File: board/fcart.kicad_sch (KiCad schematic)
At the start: 95 parts, among them J1 JTAG, J2 USB4085, J3 MSD-4-A, J4 SWD, J5 Famicom_cartridge, SW1 PTS647SM70, U1 TPS2116, U10 LCMXO2-4000HC-4TG144C, U2 USBLC6-2SC6, U3 TLV76133DCY, U4 SN74ALVC164245DGG, U5 SN74ALVC164245DGG, U6 SN74ALVC164245DGG, U7 SN74ALVC164245DGG, U8 STM32F412RET6, U9 W9864G6KH-6, Y1 ABS07-32.768KHZ-7, Y2 ABM8W-12.0000MHZ-8-B1U, Y3 ASE-50.000MHZ-LC

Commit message: implementation of sound dac
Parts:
- removed R8: 100, Resistor_SMD:R_0805_2012Metric, symbol Device:R
- added C9: 0.1u, Capacitor_SMD:C_0805_2012Metric, symbol Device:C
- added R10: 47k, Resistor_SMD:R_0805_2012Metric, symbol Device:R
- added R9: 100k, Resistor_SMD:R_0805_2012Metric, symbol Device:R
- added U4: LM321, Package_TO_SOT_SMD:SOT-23-5, symbol Amplifier_Operational:LM321
- C10: renamed from C6; value 4.7u -> 10u
- C8: renamed from C7; value 0.1u -> 10n
- renumbered C8 to C1, C1 to C11, C5 to C12, C12 to C13, C13 to C14, C14 to C15, C15 to C16, C16 to C17, C17 to C18, C18 to C19, C19 to C20, C25 to C21, C26 to C22, C20 to C23, C21 to C24, C22 to C25, C27 to C26, C23 to C27, C24 to C28, C28 to C29, C9 to C3, C29 to C30, C30 to C31, C31 to C32, C32 to C33, C33 to C34, C46 to C35, C34 to C36, C35 to C37, C36 to C38, C37 to C39, C10 to C4, C38 to C40, C39 to C41, C40 to C42, C41 to C43, C42 to C44, C43 to C45, C44 to C46, C45 to C47, C47 to C48, C48 to C49, C11 to C5, C49 to C50, C50 to C51, C3 to C6, C4 to C7, J2 to J1, J3 to J2, J4 to J3, J1 to J4, R2 to R1, R10 to R11, R11 to R12, R4 to R2, R6 to R4, R9 to R6, R1 to R7, R7 to R8, U2 to U1, U9 to U11, U3 to U2, U1 to U3, U4 to U5, U5 to U6, U6 to U7, U7 to U8, U8 to U9
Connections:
- net GND: now also U7.43 (1A3), C9.1, R9.2, U4.2 (V-)
- net PPU_A0: now also U10.87 (PR10D/BANK1/C); no longer U10.89 (PR10C/BANK1/T)
- net PPU_A1: now also U10.85 (PR13B/BANK1/C/DQS1N); no longer U10.86 (PR13A/BANK1/T/DQS1)
- net PPU_A10: now also U10.82 (PR15A/BANK1/T/DQ1); no longer U10.83 (PR14B/BANK1/C/DQ1)
- net PPU_A11: now also U10.84 (PR14A/BANK1/T/DQ1); no longer U10.85 (PR13B/BANK1/C/DQS1N)
- net PPU_A12: now also U10.86 (PR13A/BANK1/T/DQS1); no longer U10.87 (PR10D/BANK1/C)
- net PPU_A13: now also U10.89 (PR10C/BANK1/T); no longer U10.91 (PR10B/BANK1/C/PCLKC1_0/DQ0)
- net PPU_A2: now also U10.83 (PR14B/BANK1/C/DQ1); no longer U10.84 (PR14A/BANK1/T/DQ1)
- net PPU_A3: now also U10.81 (PR15B/BANK1/C/DQ1); no longer U10.82 (PR15A/BANK1/T/DQ1)
- net PPU_A4: now also U10.77 (PR16B/BANK1/C/DQ1); no longer U10.78 (PR16A/BANK1/T/DQ1)
- net PPU_A5: now also U10.75 (PR18B/BANK1/C/DQ1); no longer U10.76 (PR18A/BANK1/T/DQ1)
- net PPU_A6: now also U10.73 (PR19B/BANK1/C/DQ1); no longer U10.74 (PR19A/BANK1/T/DQ1)
- net PPU_A7: now also U10.74 (PR19A/BANK1/T/DQ1); no longer U10.75 (PR18B/BANK1/C/DQ1)
- net PPU_A8: now also U10.76 (PR18A/BANK1/T/DQ1); no longer U10.77 (PR16B/BANK1/C/DQ1)
- net PPU_A9: now also U10.78 (PR16A/BANK1/T/DQ1); no longer U10.81 (PR15B/BANK1/C/DQ1)
- net PPU_D0: now also U10.91 (PR10B/BANK1/C/PCLKC1_0/DQ0); no longer U10.93 (PR9B/BANK1/C/DQS0N)
- net PPU_D1: now also U10.94 (PR9A/BANK1/T/DQS0); no longer U10.95 (PR8B/BANK1/C/DQ0)
- net PPU_D2: now also U10.96 (PR8A/BANK1/T/DQ0); no longer U10.97 (PR6B/BANK1/C/DQ0)
- net PPU_D3: now also U10.98 (PR6A/BANK1/T/DQ0); no longer U10.99 (PR5B/BANK1/C/DQ0)
- net PPU_D4: now also U10.99 (PR5B/BANK1/C/DQ0); no longer U10.100 (PR5A/BANK1/T/DQ0)
- net PPU_D5: now also U10.97 (PR6B/BANK1/C/DQ0); no longer U10.98 (PR6A/BANK1/T/DQ0)
- net PPU_D6: now also U10.95 (PR8B/BANK1/C/DQ0); no longer U10.96 (PR8A/BANK1/T/DQ0)
- net PPU_D7: now also U10.93 (PR9B/BANK1/C/DQS0N); no longer U10.94 (PR9A/BANK1/T/DQS0)
- net PPU_DIR: now also U10.100 (PR5A/BANK1/T/DQ0); no longer U10.103 (PR4C/BANK1)
- net PPU_RD: now also U10.69 (PB29B/BANK2/C); no longer U10.73 (PR19B/BANK1/C/DQ1)
- net PPU_WR: now also U10.68 (PB29A/BANK2/T); no longer U10.69 (PB29B/BANK2/C)
- net SDRAM_CAS: now also U10.23 (PL14A/BANK4/T); no longer U10.24 (PL14B/BANK4/C)
- net SDRAM_CS: now also U10.21 (PL13A/BANK4/T); no longer U10.22 (PL13B/BANK4/C)
- net SDRAM_DQ0: now also U10.11 (PL8A/BANK5/T); no longer U10.12 (PL8B/BANK5/C)
- net SDRAM_DQ1: now also U10.12 (PL8B/BANK5/C); no longer U10.13 (PL9A/BANK4/T)
- net SDRAM_DQ10: now also U10.3 (PL4A/BANK5/T/L_GPLLT_IN); no longer U10.4 (PL4B/BANK5/C/L_GPLLC_IN)
- net SDRAM_DQ11: now also U10.4 (PL4B/BANK5/C/L_GPLLC_IN); no longer U10.5 (PL6A/BANK5/T/PCLKT5_0)
- net SDRAM_DQ12: now also U10.5 (PL6A/BANK5/T/PCLKT5_0); no longer U10.6 (PL6B/BANK5/C/PCLKC5_0)
- net SDRAM_DQ13: now also U10.6 (PL6B/BANK5/C/PCLKC5_0); no longer U10.9 (PL7A/BANK5/T)
- net SDRAM_DQ14: now also U10.9 (PL7A/BANK5/T); no longer U10.10 (PL7B/BANK5/C)
- net SDRAM_DQ15: now also U10.10 (PL7B/BANK5/C); no longer U10.11 (PL8A/BANK5/T)
- net SDRAM_DQ2: now also U10.13 (PL9A/BANK4/T); no longer U10.14 (PL9B/BANK4/C)
- net SDRAM_DQ3: now also U10.14 (PL9B/BANK4/C); no longer U10.15 (PL10A/BANK4/T)
- net SDRAM_DQ4: now also U10.15 (PL10A/BANK4/T); no longer U10.17 (PL10B/BANK4/C)
- net SDRAM_DQ5: now also U10.17 (PL10B/BANK4/C); no longer U10.19 (PL10C/BANK4/T/PCLKT4_0)
- net SDRAM_DQ6: now also U10.19 (PL10C/BANK4/T/PCLKT4_0); no longer U10.20 (PL10D/BANK4/C/PCLKC4_0)
- net SDRAM_DQ7: now also U10.20 (PL10D/BANK4/C/PCLKC4_0); no longer U10.21 (PL13A/BANK4/T)
- net SDRAM_DQ8: now also U10.1 (PL3A/BANK5/T/L_GPLLT_FB); no longer U10.2 (PL3B/BANK5/C/L_GPLLC_FB)
- net SDRAM_DQ9: now also U10.2 (PL3B/BANK5/C/L_GPLLC_FB); no longer U10.3 (PL4A/BANK5/T/L_GPLLT_IN)
- net SDRAM_LDQM: now also U10.25 (PL16A/BANK3/T); no longer U10.26 (PL16B/BANK3/C)
- net SDRAM_RAS: now also U10.22 (PL13B/BANK4/C); no longer U10.23 (PL14A/BANK4/T)
- net SDRAM_UDQM: now also U10.119 (PT23D/BANK0/C/PROGRAMN); no longer U10.1 (PL3A/BANK5/T/L_GPLLT_FB)
- net SDRAM_WE: now also U10.24 (PL14B/BANK4/C); no longer U10.25 (PL16A/BANK3/T)
- net VCART: now also C9.2, U4.5 (V+)
- net at C8.1, R8.1: now also R9.1, U4.1 (+); no longer C10.1
- net SND_IN_5V renamed SND_MIX
- net SND_MIX: now also J5.46 (SND_OUT), R10.1
- net SND_OUT_5V: no longer names the net of C10.2
- net SND_OUT_5V: now also R10.2; no longer J5.46 (SND_OUT)
- removed net SND_SYN: U10.68 (PB29A/BANK2/T), U7.43 (1A3)
- net SND_SYN_5V: no longer names the net of U7.6 (1B3)
- net SND_SYN_5V: no longer R8.2
- new net: C10.1, U4.3 (-), U4.4
- new net SND_OUT: R8.2, U10.26 (PL16B/BANK3/C)
- no-connect marks 47 -> 48
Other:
- moved on the sheet: C10, C6, C7, C8, J2, J3, J4, R7, R8

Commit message: PCB: route USB VBUS signal
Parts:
- added R5: 10k, Resistor_SMD:R_0805_2012Metric, symbol Device:R
- renumbered R9 to R10, R10 to R11, R11 to R12, R12 to R13, R5 to R6, R6 to R7, R7 to R8, R8 to R9
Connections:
- net +3V3: now also R5.2
- net BTN: now also U9.17 (PA3); no longer U9.26 (PB0)
- net CIRAM_A10: now also U10.67 (PB27B/BANK2/C); no longer U10.65 (PB27A/BANK2/T)
- net CIRAM_CE: now also U10.68 (PB29A/BANK2/T); no longer U10.67 (PB27B/BANK2/C)
- net CPU_D0: now also U10.61 (PB24A/BANK2/T); no longer U10.60 (PB23B/BANK2/C)
- net CPU_D1: now also U10.60 (PB23B/BANK2/C); no longer U10.59 (PB23A/BANK2/T)
- net CPU_D2: now also U10.59 (PB23A/BANK2/T); no longer U10.58 (PB21B/BANK2/C)
- net CPU_D3: now also U10.58 (PB21B/BANK2/C); no longer U10.57 (PB21A/BANK2/T)
- net CPU_D4: now also U10.57 (PB21A/BANK2/T); no longer U10.56 (PB20B/BANK2/C/PCLKC2_1)
- net CPU_D5: now also U10.56 (PB20B/BANK2/C/PCLKC2_1); no longer U10.55 (PB20A/BANK2/T/PCLKT2_1)
- net CPU_RW: now also U10.63 (PB24D/BANK2); no longer U10.62 (PB24B/BANK2/C)
- net FPGA_IRQ: now also U10.111 (PT27B/BANK0/C/LVDS), U9.20 (PA4); no longer U10.117 (PT24A/BANK0/T/LVDS), U9.59 (PB7)
- net IRQ: now also U10.65 (PB27A/BANK2/T); no longer U10.63 (PB24D/BANK2)
- net LED: now also U9.58 (PB6); no longer U9.62 (PB9)
- net PPU_D1: now also U10.93 (PR9B/BANK1/C/DQS0N); no longer U10.94 (PR9A/BANK1/T/DQS0)
- net PPU_D2: now also U10.95 (PR8B/BANK1/C/DQ0); no longer U10.96 (PR8A/BANK1/T/DQ0)
- net PPU_D3: now also U10.97 (PR6B/BANK1/C/DQ0); no longer U10.98 (PR6A/BANK1/T/DQ0)
- net PPU_D4: now also U10.98 (PR6A/BANK1/T/DQ0); no longer U10.99 (PR5B/BANK1/C/DQ0)
- net PPU_D5: now also U10.96 (PR8A/BANK1/T/DQ0); no longer U10.97 (PR6B/BANK1/C/DQ0)
- net PPU_D6: now also U10.94 (PR9A/BANK1/T/DQS0); no longer U10.95 (PR8B/BANK1/C/DQ0)
- net PPU_D7: now also U10.92 (PR10A/BANK1/T/PCLKT1_0/DQ0); no longer U10.93 (PR9B/BANK1/C/DQS0N)
- net PPU_DIR: now also U10.99 (PR5B/BANK1/C/DQ0); no longer U10.100 (PR5A/BANK1/T/DQ0)
- net PPU_RD: now also U10.55 (PB20A/BANK2/T/PCLKT2_1); no longer U10.69 (PB29B/BANK2/C)
- net PPU_WR: now also U10.69 (PB29B/BANK2/C); no longer U10.68 (PB29A/BANK2/T)
- net QSPI_CLK: now also U10.126 (PT20C/BANK0/T/SCL/PCLKT0_0); no longer U10.92 (PR10A/BANK1/T/PCLKT1_0/DQ0)
- net QSPI_IO0: now also U9.22 (PA6); no longer U9.40 (PC9)
- net QSPI_IO1: now also U9.23 (PA7); no longer U9.51 (PC10)
- net QSPI_IO2: now also U10.114 (PT25A/BANK0/T/LVDS), U9.24 (PC4); no longer U10.111 (PT27B/BANK0/C/LVDS), U9.39 (PC8)
- net QSPI_IO3: now also U10.115 (PT24B/BANK0/C/LVDS), U9.25 (PC5); no longer U10.114 (PT25A/BANK0/T/LVDS), U9.15 (PA1)
- net QSPI_NCS: now also U10.110 (PT28C/BANK0/T/INITN), U9.52 (PC11); no longer U10.115 (PT24B/BANK0/C/LVDS), U9.58 (PB6)
- net ROMSEL: now also U10.62 (PB24B/BANK2/C); no longer U10.61 (PB24A/BANK2/T)
- net SDRAM_A11: now also U10.119 (PT23D/BANK0/C/PROGRAMN); no longer U10.120 (PT23C/BANK0/T/JTAGENB)
- net SDRAM_A6: now also U10.125 (PT20D/BANK0/C/SDA/PCLKC0_0); no longer U10.126 (PT20C/BANK0/T/SCL/PCLKT0_0)
- net SDRAM_A7: now also U10.122 (PT21A/BANK0/T/LVDS); no longer U10.125 (PT20D/BANK0/C/SDA/PCLKC0_0)
- net SDRAM_A8: now also U10.121 (PT21B/BANK0/C/LVDS); no longer U10.122 (PT21A/BANK0/T/LVDS)
- net SDRAM_A9: now also U10.120 (PT23C/BANK0/T/JTAGENB); no longer U10.121 (PT21B/BANK0/C/LVDS)
- net SDRAM_UDQM: now also U10.117 (PT24A/BANK0/T/LVDS); no longer U10.119 (PT23D/BANK0/C/PROGRAMN)
- net SD_DAT1: now also U9.40 (PC9); no longer U9.41 (PA8)
- net SD_DAT2: now also U9.51 (PC10); no longer U9.42 (PA9)
- net SPI_MISO: now also U9.10 (PC2); no longer U9.22 (PA6)
- net SPI_MOSI: now also U9.11 (PC3); no longer U9.23 (PA7)
- net SPI_NCS: now also U9.16 (PA2); no longer U9.24 (PC4)
- net SPI_SCK: now also U9.38 (PC7); no longer U9.21 (PA5)
- net VBUS: now reaches U3.8 (ST)
- net VBUS: now also U9.42 (PA9), R5.1
- no-connect marks 48 -> 46
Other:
- moved on the sheet: D1, R6, R7, SW1

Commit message: Simplify power mux and improve audio
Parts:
- removed C10: 10u, Capacitor_SMD:C_0805_2012Metric, symbol Device:C
- removed U3: TPS2116, Package_TO_SOT_SMD:SOT-583-8, symbol Power_Management:TPS2116DRL
- removed U4: LM321, Package_TO_SOT_SMD:SOT-23-5, symbol Amplifier_Operational:LM321
- added C11: 47u, Capacitor_SMD:C_1206_3216Metric, symbol Device:C
- added C8: 0.1u, Capacitor_SMD:C_0805_2012Metric, symbol Device:C
- added D1, D2: MBR120, Diode_SMD:D_SOD-123F, symbol Device:D_Schottky
- added Q1: DTC114E, Package_TO_SOT_SMD:SOT-23-3, symbol Transistor_BJT:DTC114E
- added R12: 10k, Resistor_SMD:R_0805_2012Metric, symbol Device:R
- added U3: 74LVC1G3157, Package_TO_SOT_SMD:SOT-23-6, symbol 74xGxx:74LVC1G3157
- added U4: MCP6001, Package_TO_SOT_SMD:SOT-23-5, symbol Amplifier_Operational:MCP6001-OT
- C1: renamed from C4; value 1u -> 10u
- C2: renamed from C5; value 4.7u -> 10u
- C5: renamed from C2; value 10u -> 0.1u
- R10: value 100k -> 2.2k
- R11: value 47k -> 1k
- R3: value 10k -> 5.1k
- R4: value 5.1k -> 10k
- renumbered C9 to C10, C11 to C12, C12 to C13, C13 to C14, C14 to C15, C15 to C16, C16 to C17, C17 to C18, C18 to C19, C19 to C20, C20 to C21, C21 to C22, C22 to C23, C23 to C24, C24 to C25, C25 to C26, C26 to C27, C27 to C28, C28 to C29, C1 to C3, C29 to C30, C30 to C31, C31 to C32, C32 to C33, C33 to C34, C34 to C35, C35 to C36, C36 to C37, C37 to C38, C38 to C39, C3 to C4, C39 to C40, C40 to C41, C41 to C42, C42 to C43, C43 to C44, C44 to C45, C45 to C46, C46 to C47, C47 to C48, C48 to C49, C49 to C50, C50 to C51, C51 to C52, C8 to C9, D1 to D3, R12 to R13, R13 to R14
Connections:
- net +3V3: now also R5.1, C8.2, R12.2, U3.5 (VCC); no longer R5.2
- net +5V: now also D1.1 (K), D2.1 (K)
- net CIRAM_A10: now also U10.68 (PB29A/BANK2/T); no longer U10.67 (PB27B/BANK2/C)
- net CIRAM_CE: now also U10.69 (PB29B/BANK2/C); no longer U10.68 (PB29A/BANK2/T)
- net GND: now also C8.1, Q1.2 (E), U3.2 (GND), U4.2 (V-); no longer R10.2, U5.25 (2~{OE}), U5.48 (1~{OE}), U6.25 (2~{OE}), U6.48 (1~{OE}), U7.25 (2~{OE}), U7.48 (1~{OE}), U8.25 (2~{OE}), U8.48 (1~{OE})
- net IRQ: now also U10.67 (PB27B/BANK2/C); no longer U10.65 (PB27A/BANK2/T)
- net PPU_A0: now also U10.89 (PR10C/BANK1/T); no longer U10.87 (PR10D/BANK1/C)
- net PPU_A1: now also U10.86 (PR13A/BANK1/T/DQS1); no longer U10.85 (PR13B/BANK1/C/DQS1N)
- net PPU_A10: now also U10.83 (PR14B/BANK1/C/DQ1); no longer U10.82 (PR15A/BANK1/T/DQ1)
- net PPU_A11: now also U10.85 (PR13B/BANK1/C/DQS1N); no longer U10.84 (PR14A/BANK1/T/DQ1)
- net PPU_A12: now also U10.87 (PR10D/BANK1/C); no longer U10.86 (PR13A/BANK1/T/DQS1)
- net PPU_A13: now also U10.91 (PR10B/BANK1/C/PCLKC1_0/DQ0); no longer U10.89 (PR10C/BANK1/T)
- net PPU_A2: now also U10.84 (PR14A/BANK1/T/DQ1); no longer U10.83 (PR14B/BANK1/C/DQ1)
- net PPU_A3: now also U10.82 (PR15A/BANK1/T/DQ1); no longer U10.81 (PR15B/BANK1/C/DQ1)
- net PPU_A4: now also U10.78 (PR16A/BANK1/T/DQ1); no longer U10.77 (PR16B/BANK1/C/DQ1)
- net PPU_A5: now also U10.76 (PR18A/BANK1/T/DQ1); no longer U10.75 (PR18B/BANK1/C/DQ1)
- net PPU_A6: now also U10.74 (PR19A/BANK1/T/DQ1); no longer U10.73 (PR19B/BANK1/C/DQ1)
- net PPU_A7: now also U10.75 (PR18B/BANK1/C/DQ1); no longer U10.74 (PR19A/BANK1/T/DQ1)
- net PPU_A8: now also U10.77 (PR16B/BANK1/C/DQ1); no longer U10.76 (PR18A/BANK1/T/DQ1)
- net PPU_A9: now also U10.81 (PR15B/BANK1/C/DQ1); no longer U10.78 (PR16A/BANK1/T/DQ1)
- net PPU_D0: now also U10.92 (PR10A/BANK1/T/PCLKT1_0/DQ0); no longer U10.91 (PR10B/BANK1/C/PCLKC1_0/DQ0)
- net PPU_D1: now also U10.94 (PR9A/BANK1/T/DQS0); no longer U10.93 (PR9B/BANK1/C/DQS0N)
- net PPU_D2: now also U10.96 (PR8A/BANK1/T/DQ0); no longer U10.95 (PR8B/BANK1/C/DQ0)
- net PPU_D3: now also U10.98 (PR6A/BANK1/T/DQ0); no longer U10.97 (PR6B/BANK1/C/DQ0)
- net PPU_D4: now also U10.99 (PR5B/BANK1/C/DQ0); no longer U10.98 (PR6A/BANK1/T/DQ0)
- net PPU_D5: now also U10.97 (PR6B/BANK1/C/DQ0); no longer U10.96 (PR8A/BANK1/T/DQ0)
- net PPU_D6: now also U10.95 (PR8B/BANK1/C/DQ0); no longer U10.94 (PR9A/BANK1/T/DQS0)
- net PPU_D7: now also U10.93 (PR9B/BANK1/C/DQS0N); no longer U10.92 (PR10A/BANK1/T/PCLKT1_0/DQ0)
- net PPU_DIR: now also U10.100 (PR5A/BANK1/T/DQ0); no longer U10.99 (PR5B/BANK1/C/DQ0)
- net PPU_WR: now also U10.73 (PR19B/BANK1/C/DQ1); no longer U10.69 (PB29B/BANK2/C)
- net SND_OUT: now also J5.46 (SND_OUT), U3.4; no longer R9.2, U10.26 (PL16B/BANK3/C)
- net VCART: now also D1.2 (A), Q1.1 (B), U4.5 (V+)
- net VUSB: now also D2.2 (A)
- net at R11.2: now also C11.2
- net at C9.1, R9.1: now also U4.3 (+); no longer R10.1
- net USB_DET: now reaches R3.1, R4.2
- net USB_DET: now also U9.42 (PA9)
- removed net SND_MIX: J5.45 (SND_IN), J5.46 (SND_OUT), R11.1
- removed net VBUS: R5.1, U9.42 (PA9)
- new net: C11.1, U4.1, U4.4 (-)
- new net: R10.1, R11.1, U3.3
- new net LS_OE: Q1.3 (C), R5.2, U5.25 (2~{OE}), U5.48 (1~{OE}), U6.25 (2~{OE}), U6.48 (1~{OE}), U7.25 (2~{OE}), U7.48 (1~{OE}), U8.25 (2~{OE}), U8.48 (1~{OE})
- new net PDM: R9.2, U10.26 (PL16B/BANK3/C)
- new net SND_BYP: R12.1, U10.65 (PB27A/BANK2/T), U3.6
- new net SND_IN: J5.45 (SND_IN), R10.2, U3.1
- no-connect marks 46 -> 45
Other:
- moved on the sheet: BT1, C1, C10, C12, C13, C2, C3, C4, C5, C9, D3, R11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

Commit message: pcb: redesign audio circuit with active inverting mixer
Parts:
- removed C8: 0.1u, Capacitor_SMD:C_0805_2012Metric, symbol Device:C
- removed R12: 10k, Resistor_SMD:R_0805_2012Metric, symbol Device:R
- removed U3: 74LVC1G3157, Package_TO_SOT_SMD:SOT-23-6, symbol 74xGxx:74LVC1G3157
- added C11, C9: 4.7u, Capacitor_SMD:C_0805_2012Metric, symbol Device:C
- added C12: 0.1u, Capacitor_SMD:C_0805_2012Metric, symbol Device:C
- added C13: 6.8p, Capacitor_SMD:C_0805_2012Metric, symbol Device:C
- added JP1: SND-IN-OUT, Jumper:SolderJumper-2_P1.3mm_Open_RoundedPad1.0x1.5mm, symbol Jumper:SolderJumper_2_Open
- added R10, R14: 10k, Resistor_SMD:R_0805_2012Metric, symbol Device:R
- added R11: 5.1k, Resistor_SMD:R_0805_2012Metric, symbol Device:R
- added R13: 100k, Resistor_SMD:R_0805_2012Metric, symbol Device:R
- C10: value 0.1u -> 4.7u
- R12: renamed from R10; value 2.2k -> 100k
- R15: renamed from R11; value 1k -> 10k
- renumbered C11 to C14, C12 to C15, C13 to C16, C14 to C17, C15 to C18, C16 to C19, C17 to C20, C18 to C21, C19 to C22, C20 to C23, C21 to C24, C22 to C25, C23 to C26, C24 to C27, C25 to C28, C26 to C29, C27 to C30, C28 to C31, C29 to C32, C30 to C33, C31 to C34, C32 to C35, C33 to C36, C34 to C37, C35 to C38, C36 to C39, C37 to C40, C38 to C41, C39 to C42, C40 to C43, C41 to C44, C42 to C45, C43 to C46, C44 to C47, C45 to C48, C46 to C49, C47 to C50, C48 to C51, C49 to C52, C50 to C53, C51 to C54, C52 to C55, C9 to C8, R13 to R16, R14 to R17, U11 to U10, U4 to U3, U5 to U4, U6 to U5, U7 to U6, U8 to U7, U9 to U8, U10 to U9
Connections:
- net SND_BYP is gone; now on net IRQ: U9.65 (PB27A/BANK2/T)
- net +3V3: now also R12.2, U3.5 (V+), C12.2
- net CIRAM_A10: now also U9.67 (PB27B/BANK2/C); no longer U9.68 (PB29A/BANK2/T)
- net CIRAM_CE: now also U9.68 (PB29A/BANK2/T); no longer U9.69 (PB29B/BANK2/C)
- net GND: now also R15.2, C11.1, C12.1, R13.1; no longer C10.1
- net IRQ: no longer U9.67 (PB27B/BANK2/C)
- net PPU_A0: now also U9.87 (PR10D/BANK1/C); no longer U9.89 (PR10C/BANK1/T)
- net PPU_A1: now also U9.85 (PR13B/BANK1/C/DQS1N); no longer U9.86 (PR13A/BANK1/T/DQS1)
- net PPU_A10: now also U9.82 (PR15A/BANK1/T/DQ1); no longer U9.83 (PR14B/BANK1/C/DQ1)
- net PPU_A11: now also U9.84 (PR14A/BANK1/T/DQ1); no longer U9.85 (PR13B/BANK1/C/DQS1N)
- net PPU_A12: now also U9.86 (PR13A/BANK1/T/DQS1); no longer U9.87 (PR10D/BANK1/C)
- net PPU_A13: now also U9.89 (PR10C/BANK1/T); no longer U9.91 (PR10B/BANK1/C/PCLKC1_0/DQ0)
- net PPU_A2: now also U9.83 (PR14B/BANK1/C/DQ1); no longer U9.84 (PR14A/BANK1/T/DQ1)
- net PPU_A3: now also U9.81 (PR15B/BANK1/C/DQ1); no longer U9.82 (PR15A/BANK1/T/DQ1)
- net PPU_A4: now also U9.77 (PR16B/BANK1/C/DQ1); no longer U9.78 (PR16A/BANK1/T/DQ1)
- net PPU_A5: now also U9.75 (PR18B/BANK1/C/DQ1); no longer U9.76 (PR18A/BANK1/T/DQ1)
- net PPU_A6: now also U9.73 (PR19B/BANK1/C/DQ1); no longer U9.74 (PR19A/BANK1/T/DQ1)
- net PPU_A7: now also U9.74 (PR19A/BANK1/T/DQ1); no longer U9.75 (PR18B/BANK1/C/DQ1)
- net PPU_A8: now also U9.76 (PR18A/BANK1/T/DQ1); no longer U9.77 (PR16B/BANK1/C/DQ1)
- net PPU_A9: now also U9.78 (PR16A/BANK1/T/DQ1); no longer U9.81 (PR15B/BANK1/C/DQ1)
- net PPU_D0: now also U9.91 (PR10B/BANK1/C/PCLKC1_0/DQ0); no longer U9.92 (PR10A/BANK1/T/PCLKT1_0/DQ0)
- net PPU_D1: now also U9.93 (PR9B/BANK1/C/DQS0N); no longer U9.94 (PR9A/BANK1/T/DQS0)
- net PPU_D2: now also U9.95 (PR8B/BANK1/C/DQ0); no longer U9.96 (PR8A/BANK1/T/DQ0)
- net PPU_D3: now also U9.97 (PR6B/BANK1/C/DQ0); no longer U9.98 (PR6A/BANK1/T/DQ0)
- net PPU_D4: now also U9.98 (PR6A/BANK1/T/DQ0); no longer U9.99 (PR5B/BANK1/C/DQ0)
- net PPU_D5: now also U9.96 (PR8A/BANK1/T/DQ0); no longer U9.97 (PR6B/BANK1/C/DQ0)
- net PPU_D6: now also U9.94 (PR9A/BANK1/T/DQS0); no longer U9.95 (PR8B/BANK1/C/DQ0)
- net PPU_D7: now also U9.92 (PR10A/BANK1/T/PCLKT1_0/DQ0); no longer U9.93 (PR9B/BANK1/C/DQS0N)
- net PPU_DIR: now also U9.99 (PR5B/BANK1/C/DQ0); no longer U9.100 (PR5A/BANK1/T/DQ0)
- net PPU_WR: now also U9.69 (PB29B/BANK2/C); no longer U9.73 (PR19B/BANK1/C/DQ1)
- net SND_IN: now also C9.1, JP1.1 (A); no longer R12.2
- net SND_OUT: now also C14.2, R15.1, JP1.2 (B)
- net VCART: no longer C10.2, U3.5 (V+)
- net at C14.1, U3.1: now also C13.2, R14.1; no longer U3.4 (-)
- net at C8.1, R9.1: now also C10.1; no longer U3.3 (+)
- net at R12.1: now also U3.3 (+), C11.2, R13.2; no longer R15.1
- new net: C13.1, R10.1, R11.1, R14.2, U3.4 (-)
- new net: C10.2, R11.2
- new net: C9.2, R10.2
- no-connect marks 45 -> 46
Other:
- moved on the sheet: C14, C8, R12, R15, R9, U3

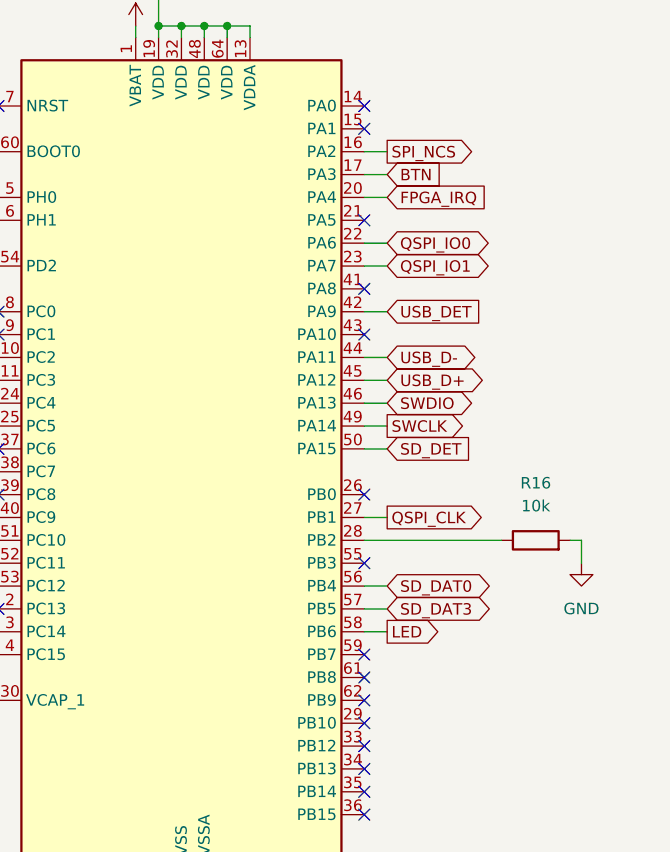
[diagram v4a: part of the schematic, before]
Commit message: Add cartridge 3D model
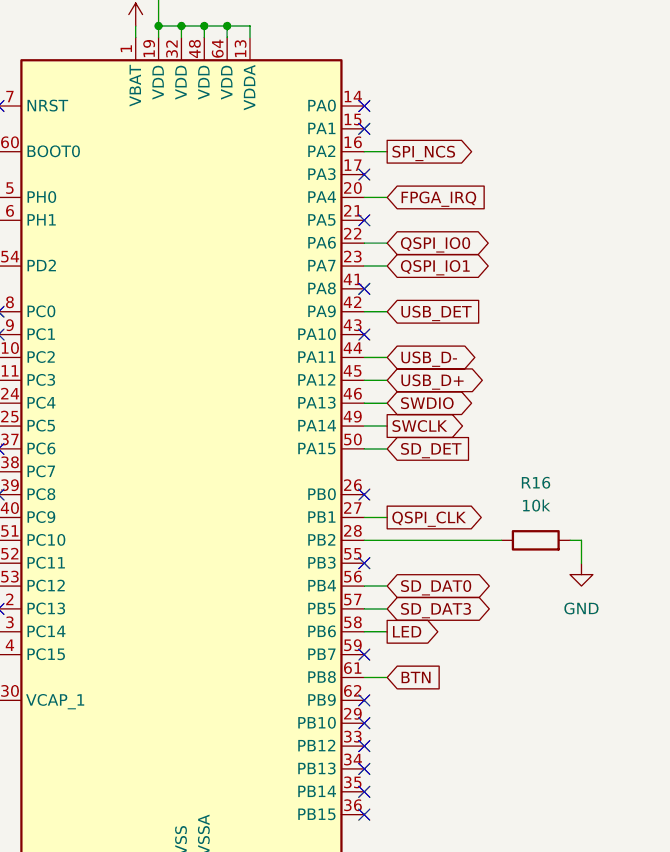
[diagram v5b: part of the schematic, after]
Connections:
- net BTN: now also U8.61 (PB8); no longer U8.17 (PA3)
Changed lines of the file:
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@@
 	)
 	(no_connect
-		(at 549.91 194.31)
+		(at 549.91 138.43)
 	)
 	(no_connect
@@
 	(wire
 		(pts
+			(xy 549.91 194.31) (xy 552.45 194.31)
+		)
+		(stroke
+			(width 0)
+			(type default)
+		)
+	)
+	(wire
+		(pts
 			(xy 391.16 165.1) (xy 397.51 165.1)
 		)
@@
 	(wire
 		(pts
-			(xy 549.91 138.43) (xy 552.45 138.43)
-		)
-		(stroke
-			(width 0)
-			(type default)
-		)
-	)
-	(wire
-		(pts
 			(xy 106.68 66.04) (xy 106.68 67.31)
 		)
@@
 	(global_label "BTN"
 		(shape input)
-		(at 552.45 138.43 0)
+		(at 552.45 194.31 0)
 		(fields_autoplaced yes)
 		(effects
@@
 		)
 		(property "Intersheetrefs" "${INTERSHEET_REFS}"
-			(at 559.0033 138.43 0)
+			(at 559.0033 194.31 0)
 			(effects
 				(font
